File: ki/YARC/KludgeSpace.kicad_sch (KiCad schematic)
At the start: 33 parts, among them J8 6-PIN FROM MCR, U100 74LS32, U101 74LS157, U139 74HC74, U140 74LS32, U149 74LS139, U150 74LS157

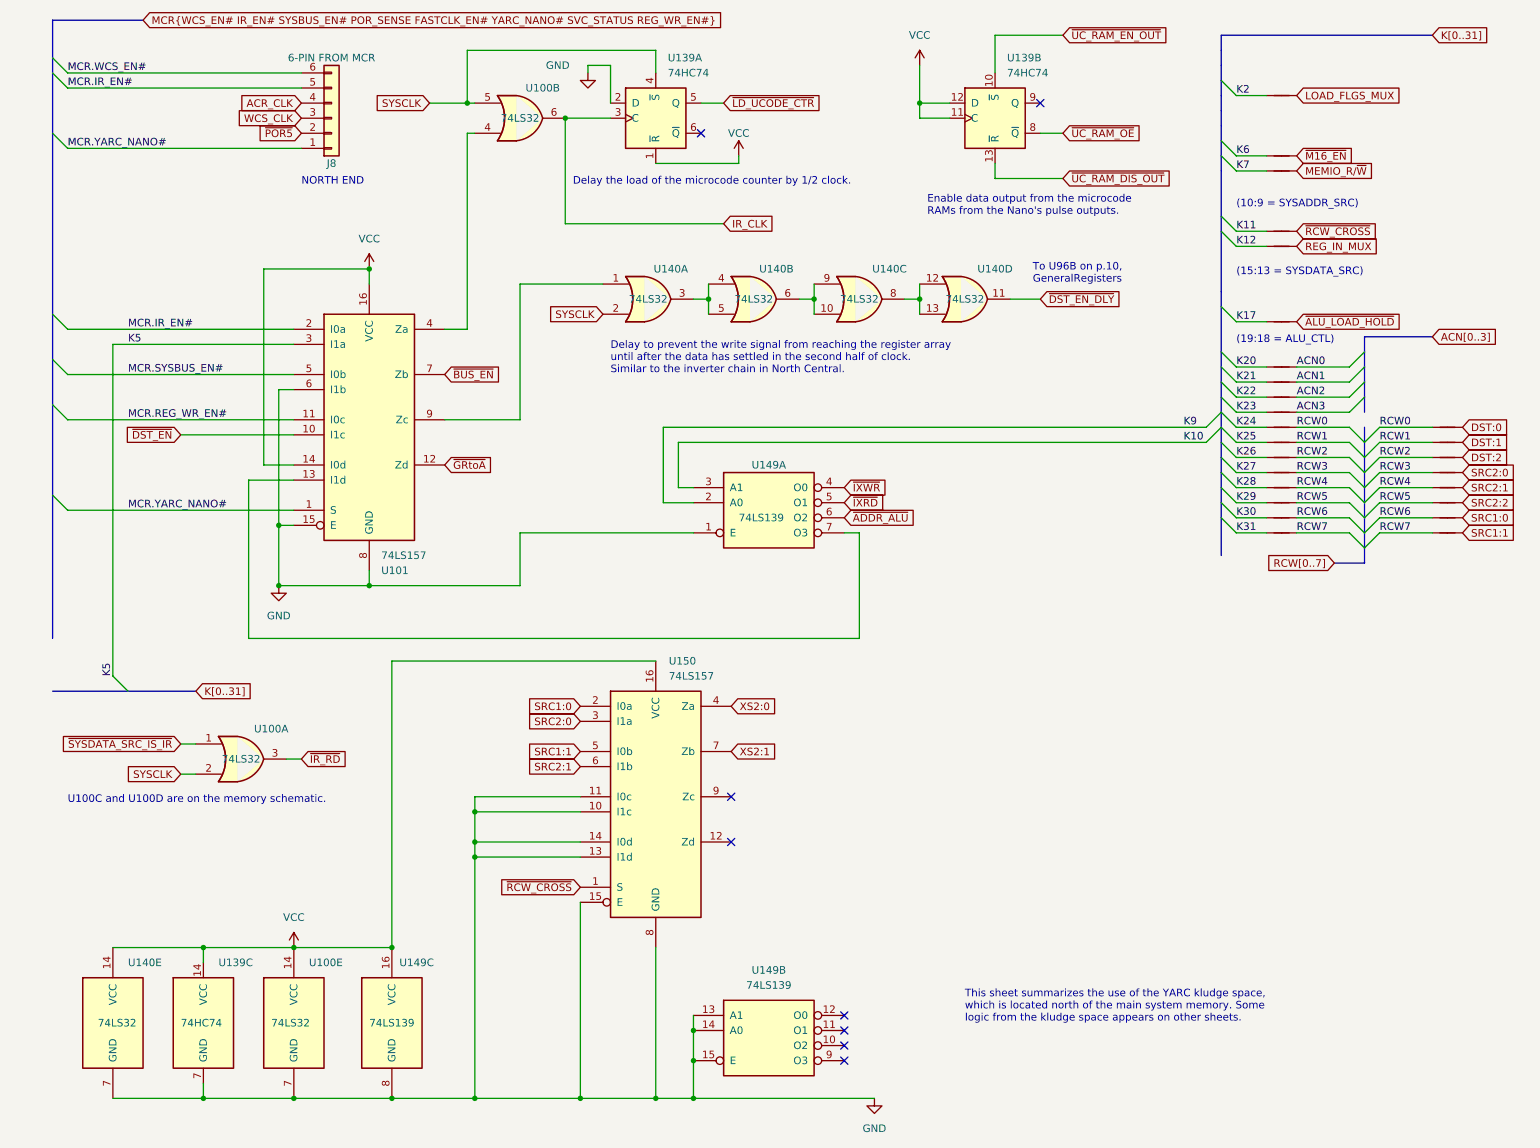
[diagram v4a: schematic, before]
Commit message: Additional minor corrections. ERC clean.
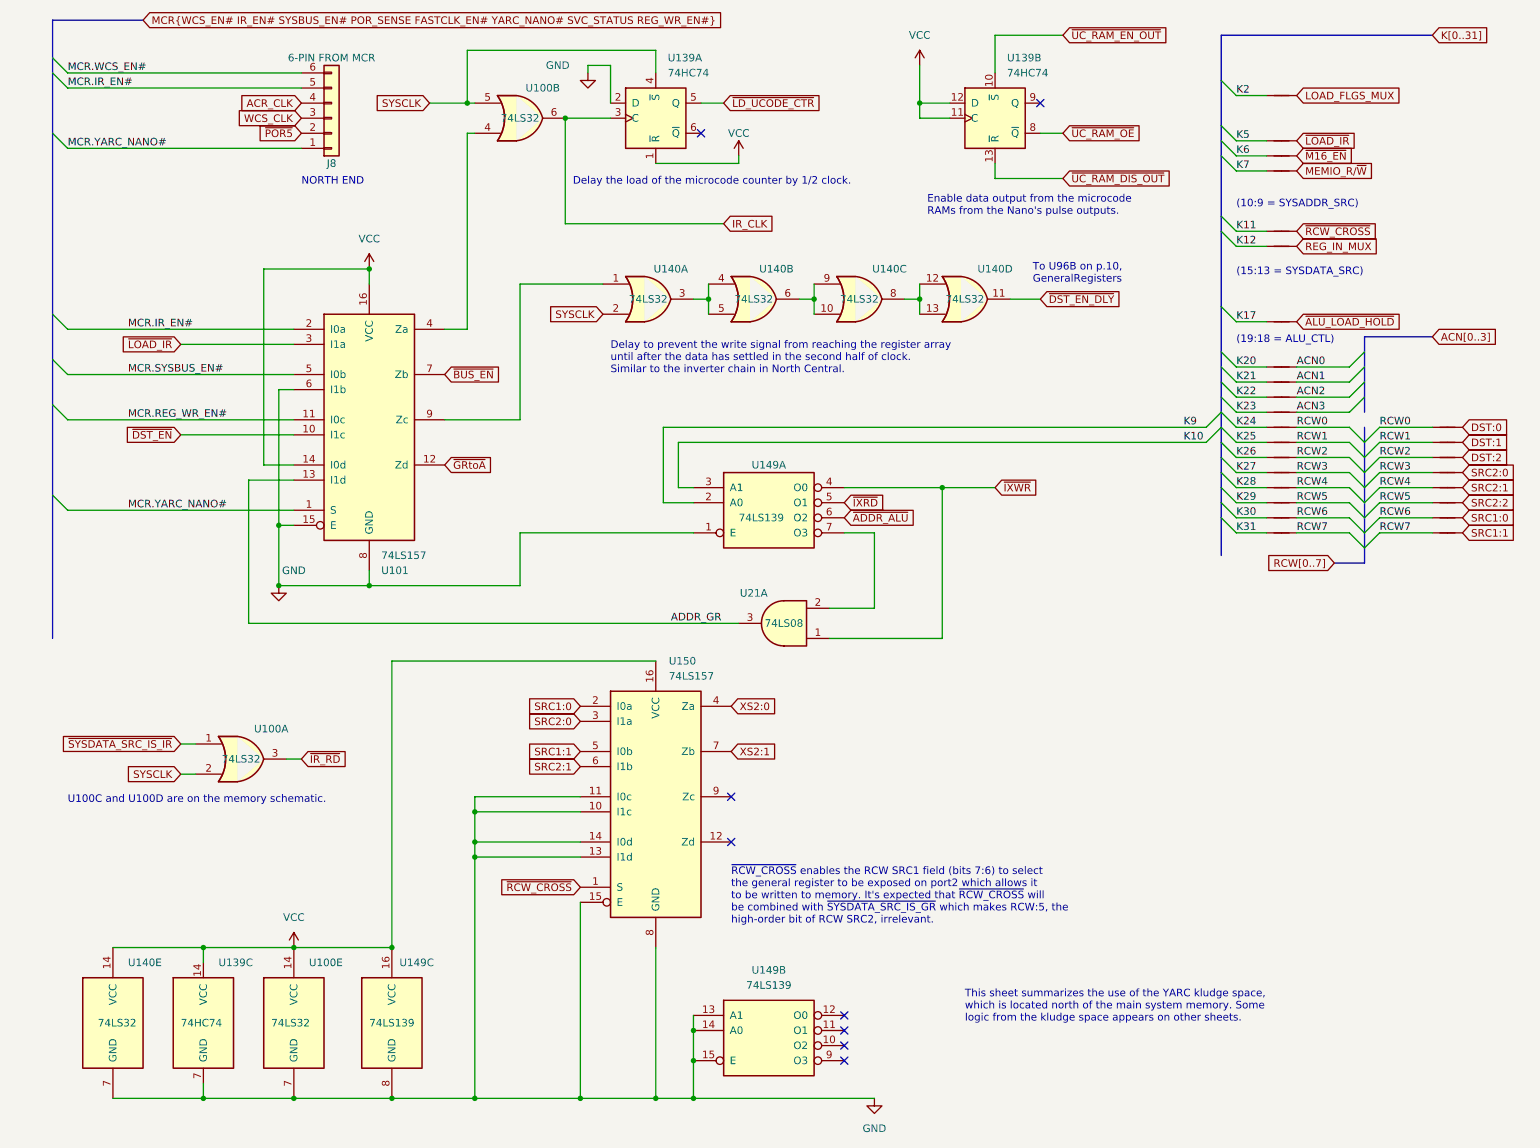
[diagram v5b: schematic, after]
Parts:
- added NT146: NetTie_2, symbol Device:NetTie_2
- added U21: 74LS08, symbol 74xx:74LS08
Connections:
- net K5: now also NT146.1; no longer U101.3 (I1a)
- net ~{IXWR}: now also U21.1
- net at U149.7 (O3): now also U21.2; no longer U101.13 (I1d)
- new net ADDR_GR: U101.13 (I1d), U21.3
- new net ~{LOAD_IR}: NT146.2, U101.3 (I1a)
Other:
- note added: "~{RCW_CROSS} enables the RCW SRC1 field (bits 7:6) to select the general register to be exposed on port2 which allows it to be written to memory. It's expected that ~{RCW_CROSS} will be combined with ~{SYSDATA_SRC_IS_GR} which makes RCW:5, the high-order bit of RCW SRC2, irrelevant."

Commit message: Revise SET# logic for LD_UCODE_CTR#. Fix minor errors with no functional consequences (schematic didn't match reality)
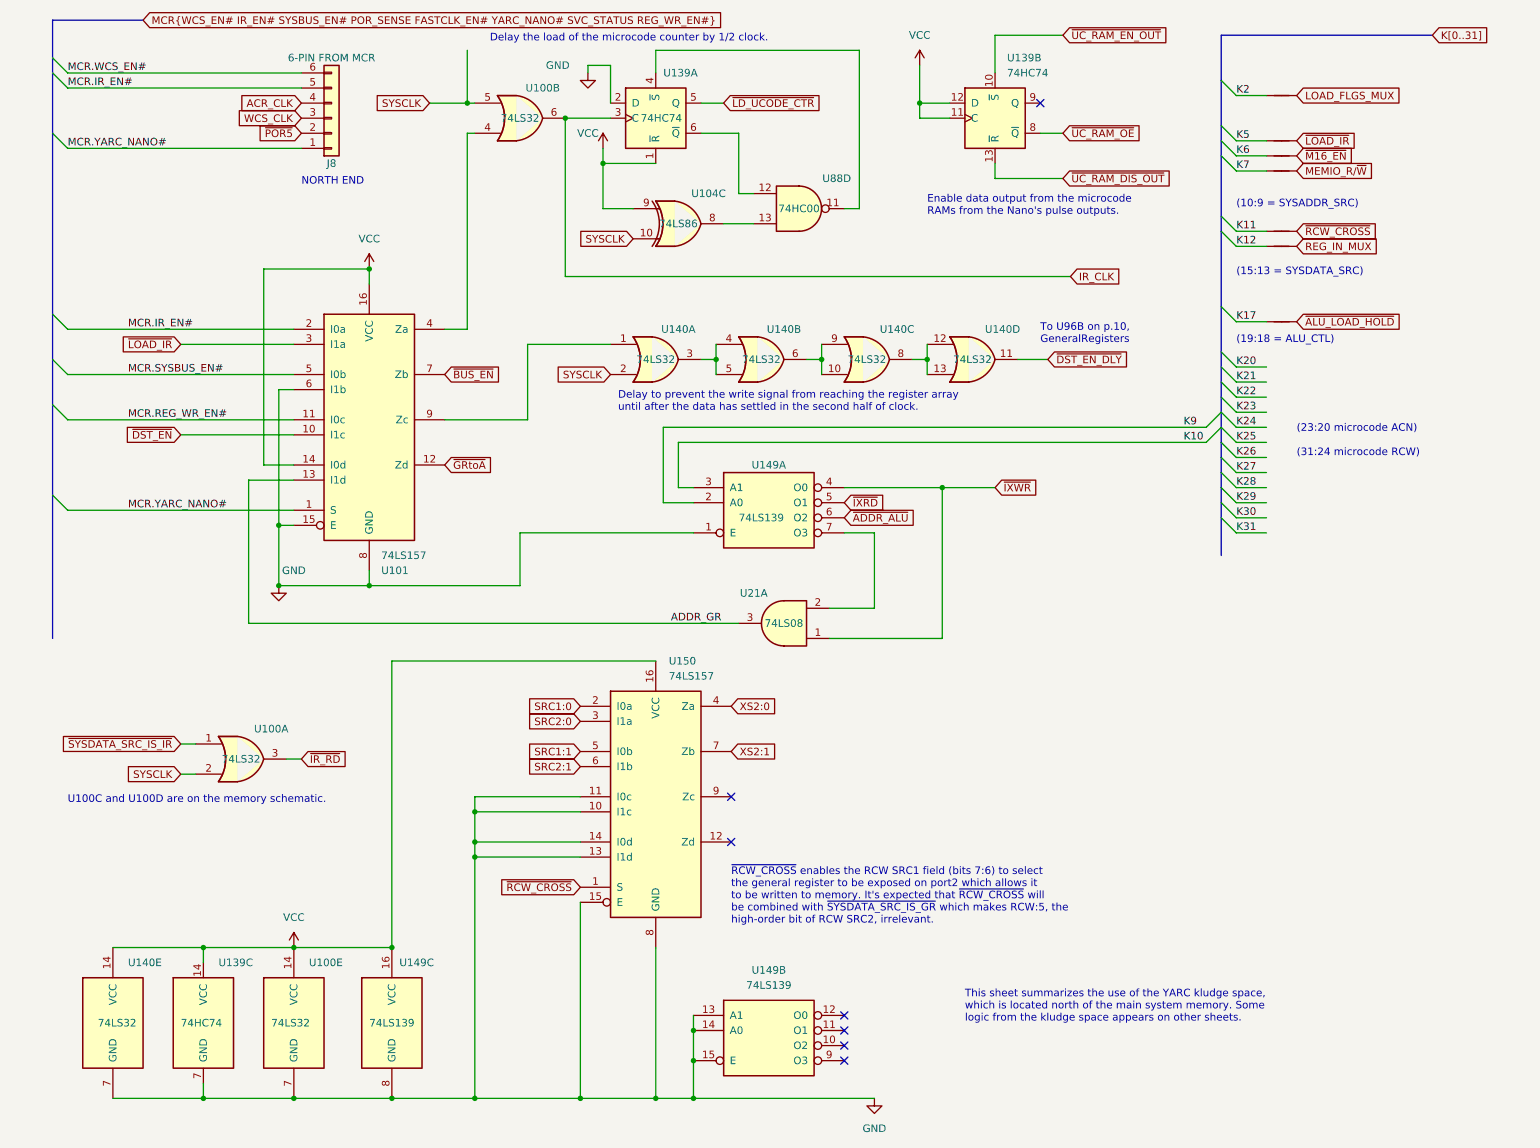
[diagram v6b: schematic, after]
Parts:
- removed NT166, NT167, NT168, NT169, NT170, NT171, NT172, NT173, NT174, NT175, NT176, NT177, NT178, NT179, NT180, NT181, NT182, NT183, NT184, NT185: NetTie_2, symbol Device:NetTie_2
- added U104: 74LS86, symbol 74xx:74LS86
- added U88: 74HC00, symbol 74xx:74HC00
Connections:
- net SYSCLK: now also U104.10; no longer U139.4 (~{S})
- net VCC: now also U104.9
- net at U139.6 (~{Q}): now also U88.12
- new net: U139.4 (~{S}), U88.11
- new net: U104.8, U88.13
- no-connect marks 8 -> 7
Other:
- note added: "(23:20 microcode ACN) (31:24 microcode RCW)"
- note added: "Delay to prevent the write signal from reaching the register array until after the data has settled in the second half of clock."
- note removed: "Delay to prevent the write signal from reaching the register array until after the data has settled in the second half of clock. Similar to the inverter chain in North Central."
- moved on the sheet: U140A, U140B, U140C, U140D

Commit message: Make main schematic match V503 schematic control signal naming and minor layout cleanup
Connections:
- net ~{ADDR_ALU} renamed ~{ALUtoA}
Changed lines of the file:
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@@
     )
   )
-  (global_label "~{ADDR_ALU}" (shape input) (at 147.32 97.79 0) (fields_autoplaced)
+  (global_label "~{ALUtoA}" (shape input) (at 147.32 97.79 0) (fields_autoplaced)
     (effects (font (size 1.27 1.27)) (justify left))
-    (property "Intersheetrefs" "${INTERSHEET_REFS}" (at 159.6186 97.79 0)
+    (property "Intersheetrefs" "${INTERSHEET_REFS}" (at 156.7157 97.79 0)
       (effects (font (size 1.27 1.27)) (justify left) hide)
     )

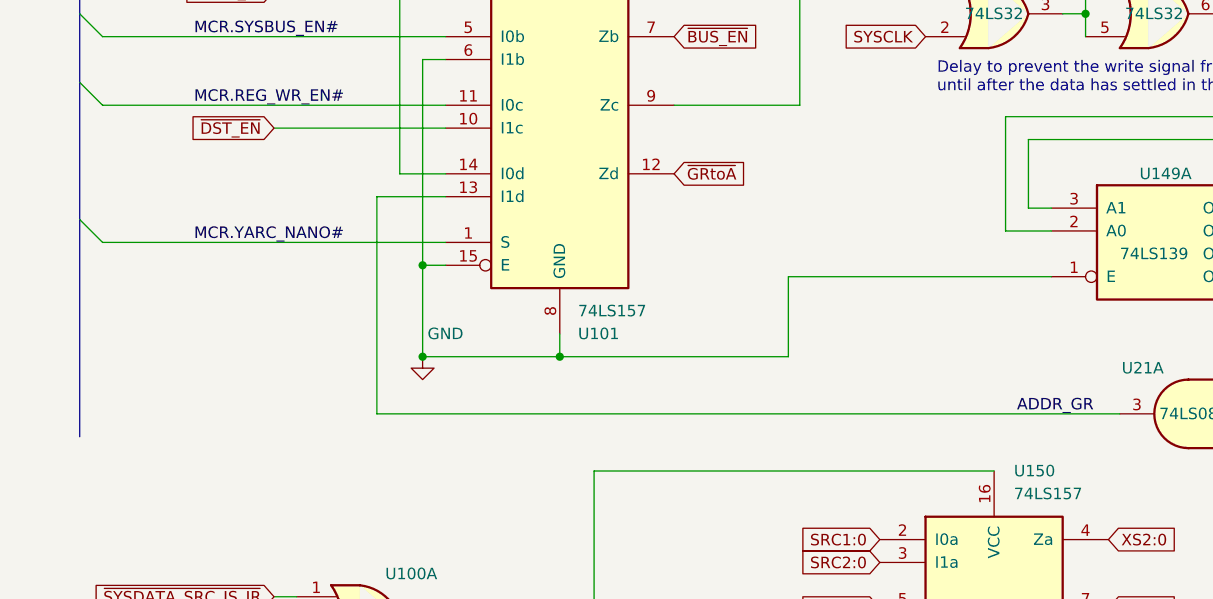
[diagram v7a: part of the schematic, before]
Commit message: Disable sysaddr_src decoder when the Nano has control of the address bus (the Nano never disables its address transceivers when it has control)
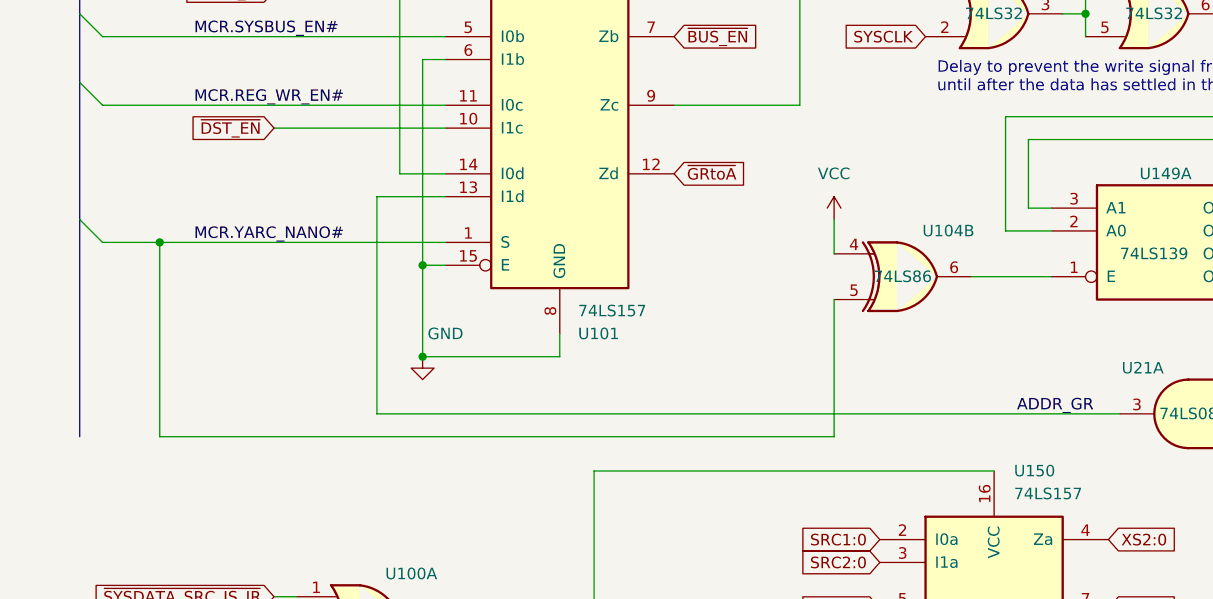
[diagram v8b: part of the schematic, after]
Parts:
- added unit 2 of U104
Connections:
- net GND: no longer U149.1 (E)
- net MCR.YARC_NANO#: now also U104.5
- net VCC: now also U104.4
- new net: U104.6, U149.1 (E)
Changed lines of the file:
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@@
   (junction (at 71.12 195.58) (diameter 0) (color 0 0 0 0)
   )
-  (junction (at 67.31 109.22) (diameter 0) (color 0 0 0 0)
-  )
   (junction (at 39.37 195.58) (diameter 0) (color 0 0 0 0)
   )
@@
   )
   (junction (at 102.87 195.58) (diameter 0) (color 0 0 0 0)
+  )
+  (junction (at 22.86 96.52) (diameter 0) (color 0 0 0 0)
   )
   (no_connect (at 180.34 27.94))
@@
     (stroke (width 0) (type default))
   )
+  (wire (pts (xy 97.79 97.79) (xy 97.79 93.98))
+    (stroke (width 0) (type default))
+  )
   (wire (pts (xy 106.68 38.1) (xy 106.68 35.56))
     (stroke (width 0) (type default))
@@
     (stroke (width 0) (type default))
   )
+  (wire (pts (xy 22.86 96.52) (xy 22.86 118.11))
+    (stroke (width 0) (type default))
+  )
   (wire (pts (xy 172.72 16.51) (xy 184.15 16.51))
     (stroke (width 0) (type default))
@@
     (stroke (width 0) (type default))
   )
+  (wire (pts (xy 97.79 118.11) (xy 22.86 118.11))
+    (stroke (width 0) (type default))
+  )
   (wire (pts (xy 213.36 80.01) (xy 218.44 80.01))
     (stroke (width 0) (type default))
@@
     (stroke (width 0) (type default))
   )
+  (wire (pts (xy 22.86 96.52) (xy 54.61 96.52))
+    (stroke (width 0) (type default))
+  )
   (wire (pts (xy 213.36 82.55) (xy 218.44 82.55))
     (stroke (width 0) (type default))
@@
     (stroke (width 0) (type default))
   )
+  (wire (pts (xy 113.03 100.33) (xy 121.92 100.33))
+    (stroke (width 0) (type default))
+  )
   (wire (pts (xy 213.36 97.79) (xy 218.44 97.79))
     (stroke (width 0) (type default))
@@
     (stroke (width 0) (type default))
   )
-  (wire (pts (xy 92.71 100.33) (xy 121.92 100.33))
-    (stroke (width 0) (type default))
-  )
   (bus (pts (xy 210.82 69.85) (xy 210.82 72.39))
     (stroke (width 0) (type default))
@@
     (stroke (width 0) (type default))
   )
-  (wire (pts (xy 92.71 109.22) (xy 67.31 109.22))
-    (stroke (width 0) (type default))
-  )
   (wire (pts (xy 38.1 140.97) (xy 35.56 140.97))
     (stroke (width 0) (type default))
   )
-  (wire (pts (xy 16.51 96.52) (xy 54.61 96.52))
-    (stroke (width 0) (type default))
-  )
-  (wire (pts (xy 92.71 100.33) (xy 92.71 109.22))
+  (wire (pts (xy 16.51 96.52) (xy 22.86 96.52))
     (stroke (width 0) (type default))
   )
@@
   )
   (wire (pts (xy 52.07 76.2) (xy 54.61 76.2))
+    (stroke (width 0) (type default))
+  )
+  (wire (pts (xy 97.79 102.87) (xy 97.79 118.11))
     (stroke (width 0) (type default))
   )
@@
     )
   )
+  (symbol (lib_id "74xx:74LS86") (at 105.41 100.33 0) (unit 2)
+    (in_bom yes) (on_board yes) (dnp no)
+    (property "Reference" "U104" (at 110.49 95.25 0)
+      (effects (font (size 1.27 1.27)))
+    )
+    (property "Value" "74LS86" (at 105.41 100.33 0)
+      (effects (font (size 1.27 1.27)))
+    )
+    (property "Footprint" "" (at 105.41 100.33 0)
+      (effects (font (size 1.27 1.27)) hide)
+    )
+    (property "Datasheet" "74xx/74ls86.pdf" (at 105.41 100.33 0)
+      (effects (font (size 1.27 1.27)) hide)
+    )
+    (pin "1")
+    (pin "2")
+    (pin "3")
+    (pin "4")
+    (pin "5")
+    (pin "6")
+    (pin "10")
+    (pin "8")
+    (pin "9")
+    (pin "11")
+    (pin "12")
+    (pin "13")
+    (pin "14")
+    (pin "7")
+    (instances
+      (project "YARC"
+        (path "/22e0f8e1-b0d7-4d47-bb7c-8ef04cd95fca/89d830c1-f0d9-4d89-9863-428a1b54ae3d"
+          (reference "U104") (unit 2)
+        )
+        (path "/22e0f8e1-b0d7-4d47-bb7c-8ef04cd95fca/a71dcb28-687f-4ebb-8f7d-60fc197ba42e"
+          (reference "U104") (unit 2)
+        )
+      )
+    )
+  )
   (symbol (lib_id "74xx:74LS139") (at 134.62 95.25 0) (unit 1)
     (in_bom yes) (on_board yes) (dnp no)
@@
         )
       )
+    )
+  )
+  (symbol (lib_id "power:VCC") (at 97.79 93.98 0) (unit 1)
+    (in_bom yes) (on_board yes) (dnp no) (fields_autoplaced)
+    (property "Reference" "#PWR0250" (at 97.79 97.79 0)
+      (effects (font (size 1.27 1.27)) hide)
+    )
+    (property "Value" "VCC" (at 97.79 88.9 0)
+      (effects (font (size 1.27 1.27)))
+    )
+    (property "Footprint" "" (at 97.79 93.98 0)
+      (effects (font (size 1.27 1.27)) hide)
+    )
+    (property "Datasheet" "" (at 97.79 93.98 0)
+      (effects (font (size 1.27 1.27)) hide)
+    )
+    (pin "1")
+    (instances
+      (project "YARC"
+        (path "/22e0f8e1-b0d7-4d47-bb7c-8ef04cd95fca/a71dcb28-687f-4ebb-8f7d-60fc197ba42e"
+          (reference "#PWR0250") (unit 1)
+        )
+      )
